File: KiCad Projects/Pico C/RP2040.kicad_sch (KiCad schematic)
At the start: 16 parts, among them U1 RP2040

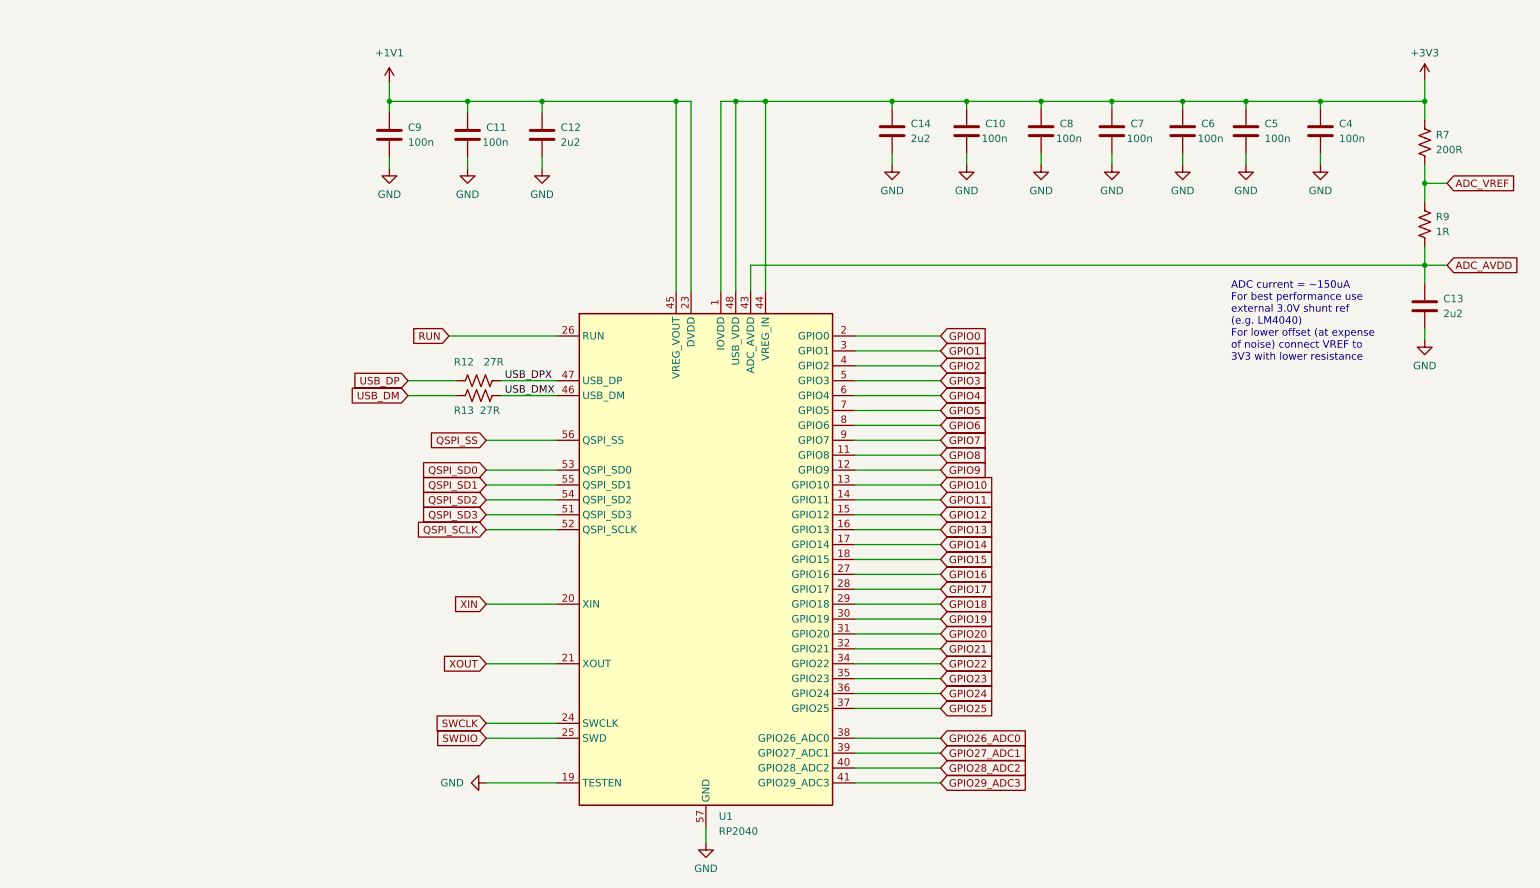
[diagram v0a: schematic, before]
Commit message: Added Pico 2
Added an initial design for the Pico 2. Also updated the original Pico C to v4 (without README update since I'm waiting on boards to ship).
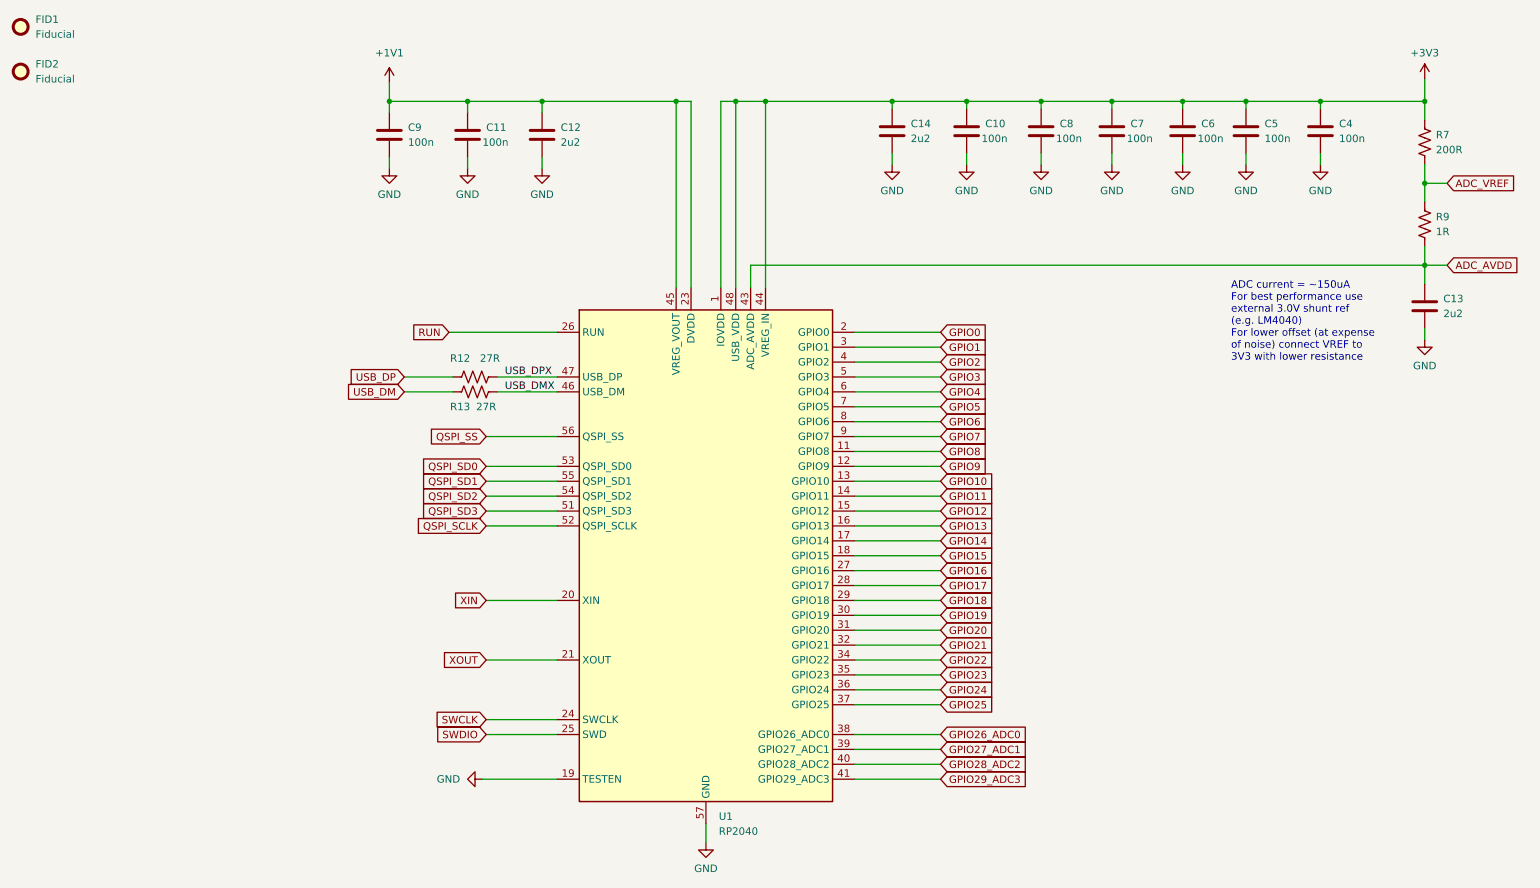
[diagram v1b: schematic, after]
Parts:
- removed U1: RP2040, Pico_C:QFN-56-1EP_7x7mm_P0.4mm_EP3.2x3.2mm_ThermalVias, symbol Pico_C:RP2040
- added FID1, FID2: Fiducial, Fiducial:Fiducial_1mm_Mask2mm, symbol Mechanical:Fiducial
- added U1: RP2040, Package_DFN_QFN:QFN-56-1EP_7x7mm_P0.4mm_EP3.2x3.2mm, symbol MCU_RaspberryPi:RP2040
- C10, C11, C4, C5, C6, C7, C8, C9: footprint Pico_C:C_0201_0603Metric -> Capacitor_SMD:C_0201_0603Metric
- R12, R13: footprint Pico_C:R_0201_0603Metric -> Resistor_SMD:R_0201_0603Metric
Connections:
- net +1V1: now also U1.23 (DVDD), U1.45 (VREG_VOUT), U1.50 (DVDD)
- net +3V3: now also U1.1 (IOVDD), U1.10 (IOVDD), U1.22 (IOVDD), U1.33 (IOVDD), U1.42 (IOVDD), U1.44 (VREG_IN), U1.48 (USB_VDD), U1.49 (IOVDD)
- net ADC_AVDD: now also U1.43 (ADC_AVDD)
- net GND: now also U1.19 (TESTEN), U1.57 (GND)
- net GPIO0: now also U1.2 (GPIO0)
- net GPIO1: now also U1.3 (GPIO1)
- net GPIO10: now also U1.13 (GPIO10)
- net GPIO11: now also U1.14 (GPIO11)
- net GPIO12: now also U1.15 (GPIO12)
- net GPIO13: now also U1.16 (GPIO13)
- net GPIO14: now also U1.17 (GPIO14)
- net GPIO15: now also U1.18 (GPIO15)
- net GPIO16: now also U1.27 (GPIO16)
- net GPIO17: now also U1.28 (GPIO17)
- net GPIO18: now also U1.29 (GPIO18)
- net GPIO19: now also U1.30 (GPIO19)
- net GPIO2: now also U1.4 (GPIO2)
- net GPIO20: now also U1.31 (GPIO20)
- net GPIO21: now also U1.32 (GPIO21)
- net GPIO22: now also U1.34 (GPIO22)
- net GPIO23: now also U1.35 (GPIO23)
- net GPIO24: now also U1.36 (GPIO24)
- net GPIO25: now also U1.37 (GPIO25)
- net GPIO26_ADC0: now also U1.38 (GPIO26_ADC0)
- net GPIO27_ADC1: now also U1.39 (GPIO27_ADC1)
- net GPIO28_ADC2: now also U1.40 (GPIO28_ADC2)
- net GPIO29_ADC3: now also U1.41 (GPIO29_ADC3)
- net GPIO3: now also U1.5 (GPIO3)
- net GPIO4: now also U1.6 (GPIO4)
- net GPIO5: now also U1.7 (GPIO5)
- net GPIO6: now also U1.8 (GPIO6)
- net GPIO7: now also U1.9 (GPIO7)
- net GPIO8: now also U1.11 (GPIO8)
- net GPIO9: now also U1.12 (GPIO9)
- net QSPI_SCLK: now also U1.52 (QSPI_SCLK)
- net QSPI_SD0: now also U1.53 (QSPI_SD0)
- net QSPI_SD1: now also U1.55 (QSPI_SD1)
- net QSPI_SD2: now also U1.54 (QSPI_SD2)
- net QSPI_SD3: now also U1.51 (QSPI_SD3)
- net QSPI_SS: now also U1.56 (QSPI_SS)
- net RUN: now also U1.26 (RUN)
- net SWCLK: now also U1.24 (SWCLK)
- net SWDIO: now also U1.25 (SWD)
- net USB_DMX: now also U1.46 (USB_DM)
- net USB_DPX: now also U1.47 (USB_DP)
- net XIN: now also U1.20 (XIN)
- net XOUT: now also U1.21 (XOUT)
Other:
- moved on the sheet: R12, R13
